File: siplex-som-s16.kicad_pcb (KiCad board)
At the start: 8 copper layers, 31.6 x 31.6 mm, 64 parts, among them J1 RFShield_OnePiece, J5 Conn_01x22, J7 Conn_01x22, J8 Conn_01x22, J9 Conn_01x22, U1 STM32H743IIKx, U2 IS42S16160J-6BLI, U3 W25Q32JVZP, U5 W25Q32JVZP, U7 TPS562200, Y1 25MHz, Y2 32.768KHz

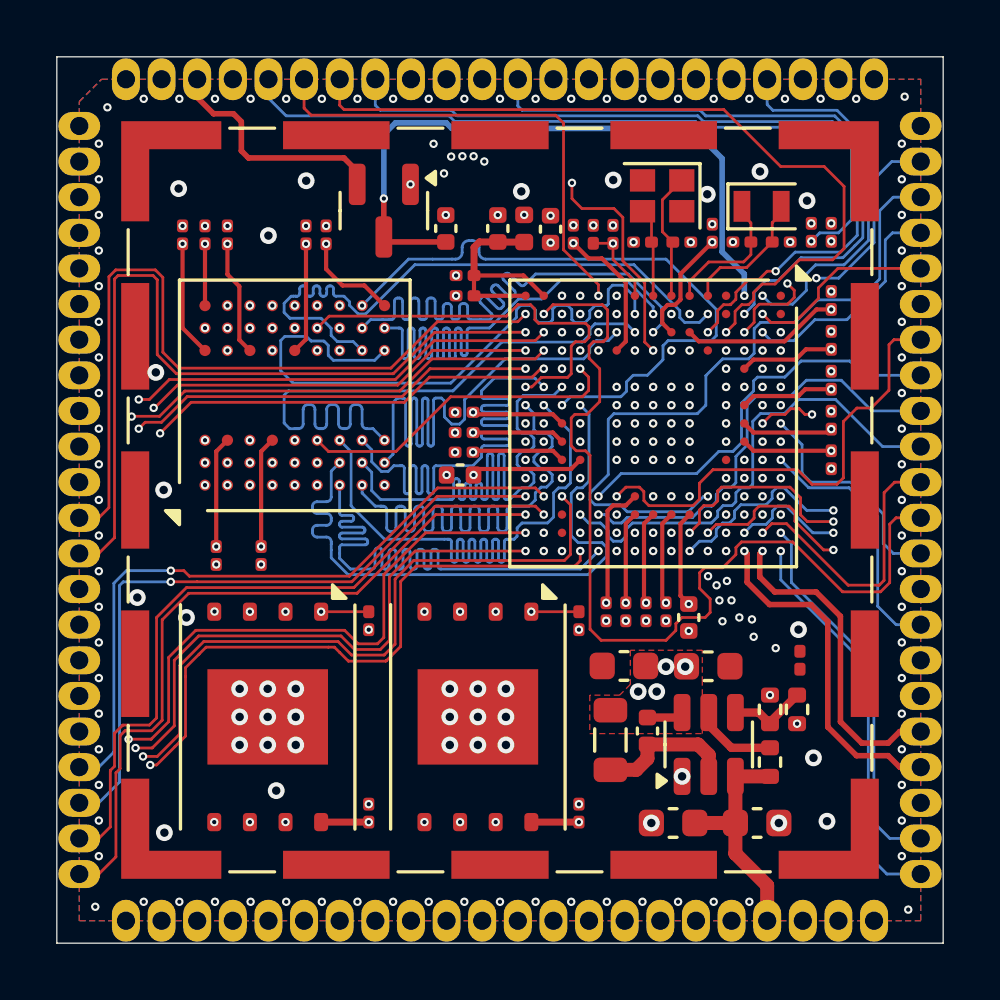
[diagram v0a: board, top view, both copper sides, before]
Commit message: Adding JLCPCB Part #
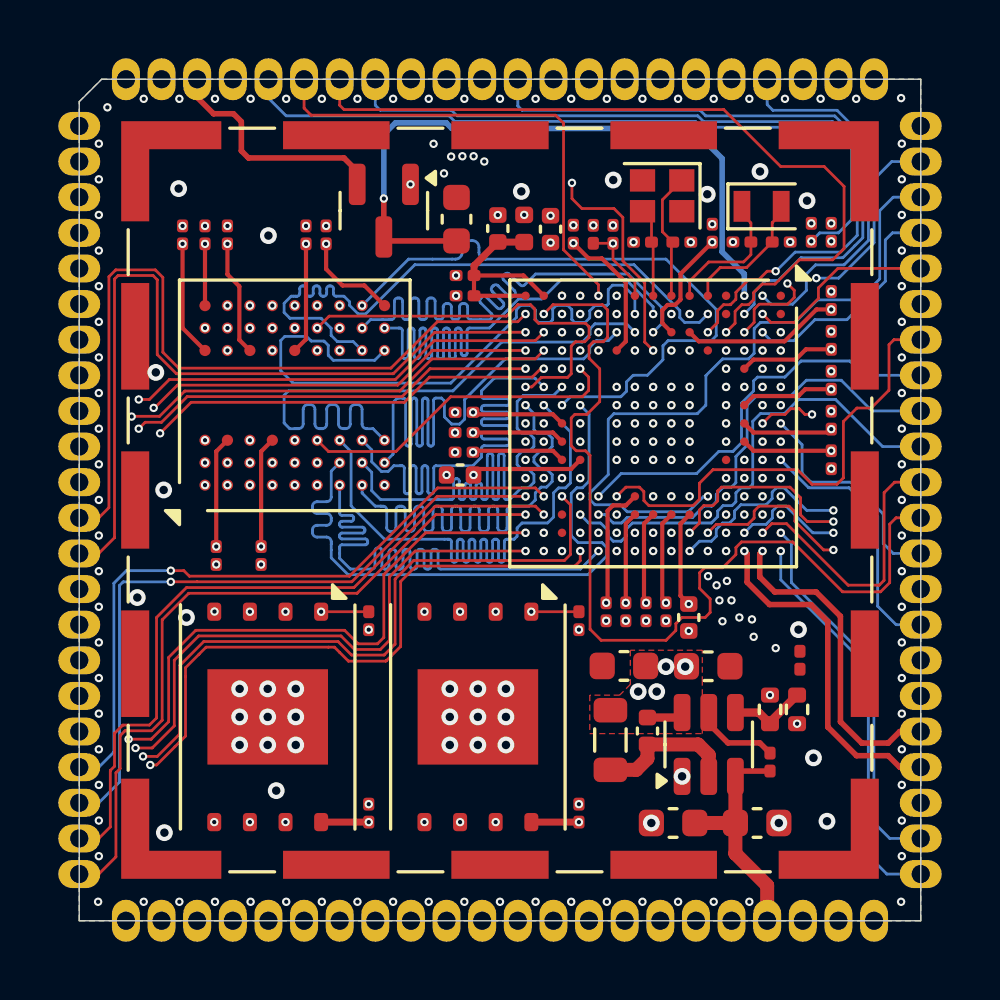
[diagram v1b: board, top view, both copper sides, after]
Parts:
- C10: footprint Capacitor_SMD:C_0402_1005Metric -> Capacitor_SMD:C_0603_1608Metric
- C43: value 100n -> 100n/0402
- L2: value 2u2 -> 2u2H
- R6: footprint Resistor_SMD:R_0402_1005Metric -> Resistor_SMD:R_0201_0603Metric
- moved C10 0.50 mm to (138.8, 88.1)
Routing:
- net GND: vias 208 -> 206
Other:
- board size 31.6 x 31.6 mm -> 30 x 30 mm

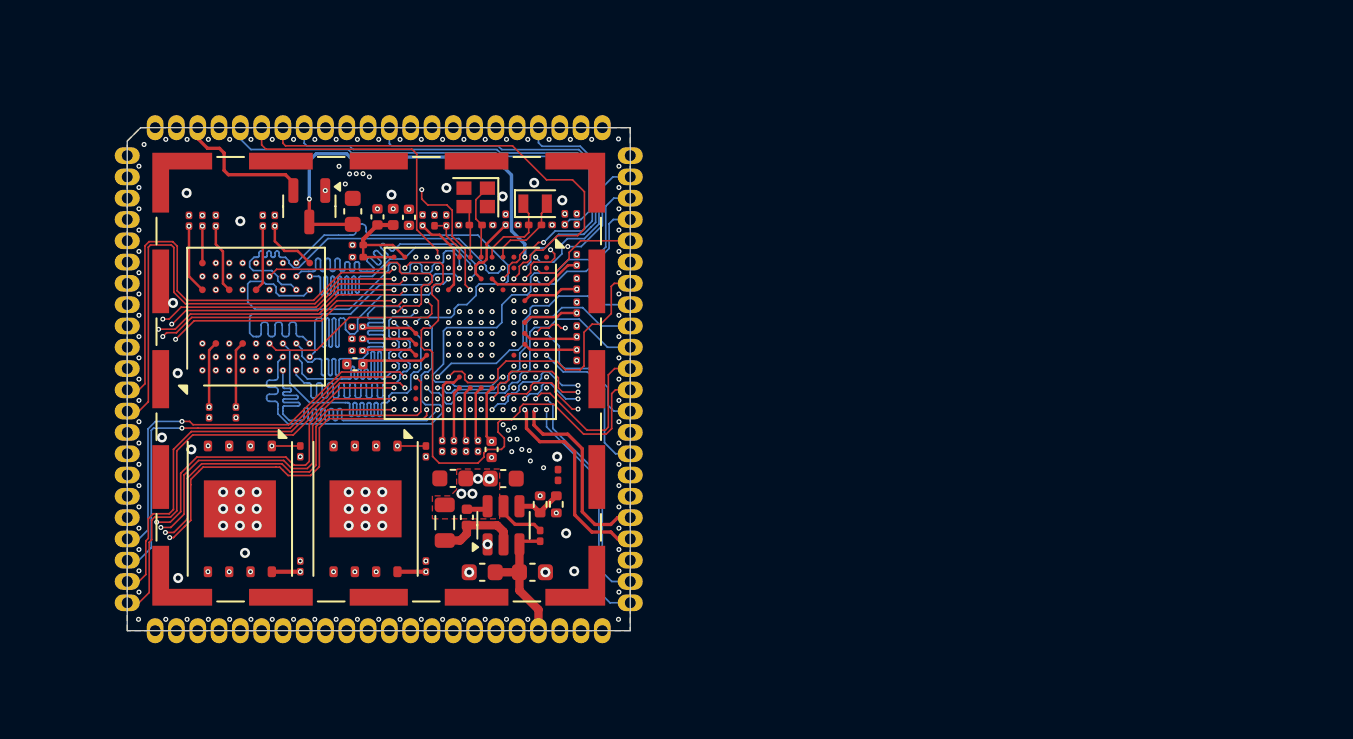
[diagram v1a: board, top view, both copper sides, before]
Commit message: Optimize layout with lowest impedance as possible
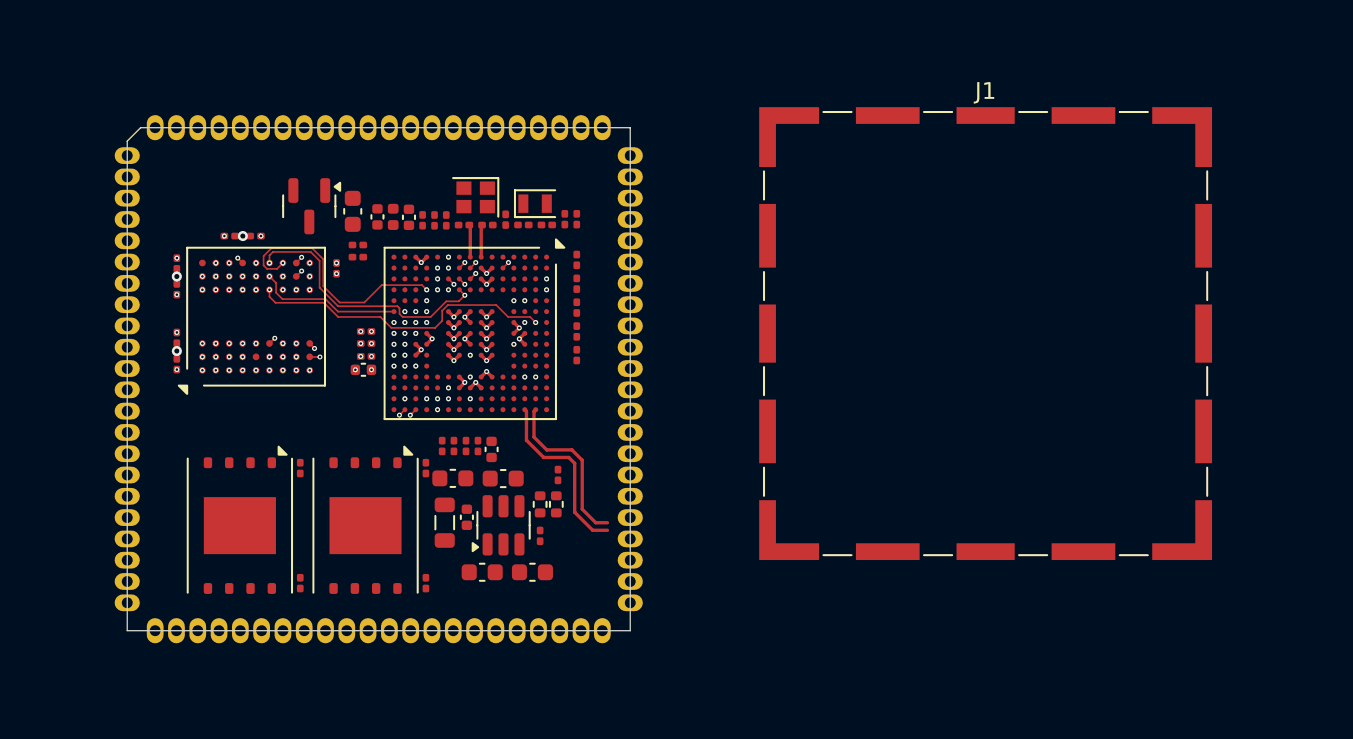
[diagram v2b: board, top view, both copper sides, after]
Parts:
- C4, C5: value 22p -> 12p
- C6, C7: value 22p -> 10p
- moved J1 36.3 mm to (176.5, 95.4), turned to 0 degrees
- moved C29 5.67 mm to (128.3, 95.6), turned to -90 degrees
- moved C28 4.65 mm to (137.8, 91.5), turned to 90 degrees
- moved C32 4.15 mm to (128.3, 92.7), turned to 90 degrees
- moved C26 3.46 mm to (128.3, 97.2)
- moved C33 2.97 mm to (128.3, 91.2)
- moved C27 1.24 mm to (131.4, 89.5), turned to 0 degrees
- moved C30 1.01 mm to (133.0, 89.5), turned to 180 degrees
- moved C31 1.00 mm to (135.6, 110.2)
- moved C38 1.00 mm to (143.1, 110.2)
- moved R4 1.00 mm to (135.6, 103.4)
- moved R5 1.00 mm to (143.1, 103.4)
- moved U3 1.00 mm to (132.0, 106.8)
- moved U5 1.00 mm to (139.5, 106.8)
- moved C11 0.63 mm to (139.6, 96.7)
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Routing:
- net +3V3: track 81.9 -> 7.36 mm, vias 35 -> 22
- net /Castellated_holes/LTDC_CLK: track 40.9 -> 0.00 mm, vias 1 -> 0
- net PB7: track 39.6 -> 0.00 mm, vias 1 -> 0
- net PB9: track 39.2 -> 0.00 mm, vias 1 -> 0
- net PB5: track 39.1 -> 0.00 mm, vias 1 -> 0
- net PB8: track 38.2 -> 0.00 mm, vias 1 -> 0
- net /MCU/~{FLASH_BK2_CS}: track 37.1 -> 0.00 mm, vias 2 -> 0
- net /MCU/BOOT0: track 34.0 -> 0.00 mm, vias 2 -> 0
- net /MCU/FLASH_BK2_IO0: track 33.8 -> 0.00 mm, vias 2 -> 0
- net /MCU/~{FLASH_BK1_CS}: track 33.8 -> 0.00 mm, vias 2 -> 0
- net /Castellated_holes/LTDC_R1: track 33.8 -> 0.00 mm, vias 1 -> 0
- net /MCU/FLASH_BK2_IO1: track 33.8 -> 0.00 mm, vias 2 -> 0
- net /MCU/FLASH_BK2_IO3: track 33.7 -> 0.00 mm, vias 2 -> 0
- net /MCU/FLASH_BK2_IO2: track 33.7 -> 0.00 mm, vias 2 -> 0
- net PD7: track 32.7 -> 0.00 mm, vias 2 -> 0
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- removed copper zone on F.Cu, net +3V3
- removed copper zone on B.Cu, net GND
- removed copper zone on F.Cu, net GND
- removed copper zone on In1.Cu, net GND
- removed copper zone on In3.Cu, net GND
- removed copper zone on In4.Cu, net GND
- removed copper zone on In6.Cu, net GND

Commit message: Finished LTDC tracks
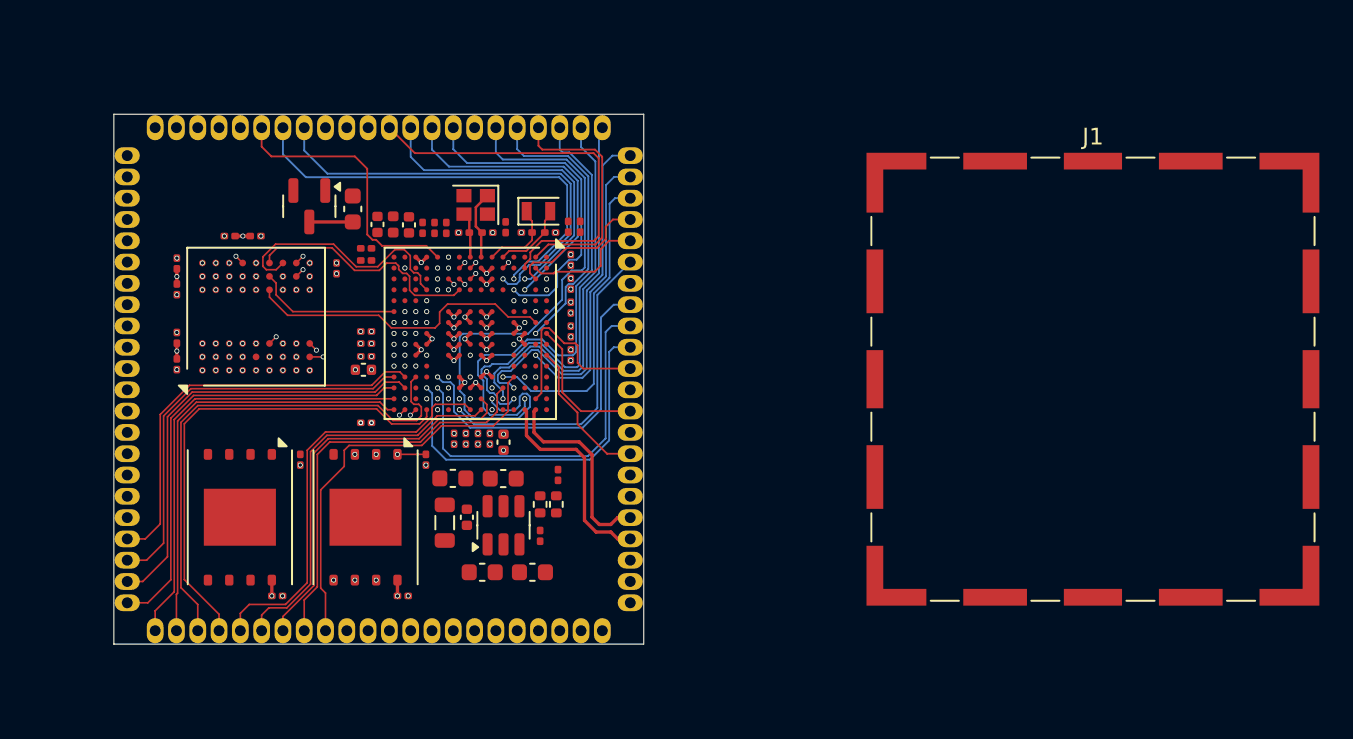
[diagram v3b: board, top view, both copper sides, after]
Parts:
- added R9: 22R, Resistor_SMD:R_0201_0603Metric, F.Cu at (139.6, 100.7)
- moved C38 8.90 mm to (134.3, 111.0), turned to 0 degrees
- moved R4 7.51 mm to (143.1, 102.9)
- moved R5 7.51 mm to (135.6, 102.9)
- moved U3 7.51 mm to (139.5, 106.3)
- moved U5 7.51 mm to (132.0, 106.3)
- moved J1 6.95 mm to (182.9, 98.1)
- moved C31 6.16 mm to (141.7, 111.0), turned to 0 degrees
- moved C2 0.83 mm to (147.8, 101.8)
- moved C17 0.83 mm to (144.8, 101.6)
- moved C18 0.83 mm to (145.5, 101.6)
- moved C22 0.83 mm to (146.2, 101.6)
- moved C23 0.83 mm to (146.9, 101.6)
- moved C39 0.53 mm to (139.6, 91.0)
- moved C9 0.53 mm to (139.6, 90.3)
- moved C6 0.49 mm to (150.5, 89.3)
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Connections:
- U3 pad 6: /MCU/FLASH_CLK -> Net-(U3-CLK)
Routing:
- net /Castellated_holes/LTDC_CLK: track 0.00 -> 37.5 mm, vias 0 -> 1
- net /Castellated_holes/LTDC_B2: track 0.00 -> 35.6 mm, vias 0 -> 1
- net PH7: track 0.00 -> 30.9 mm
- net PD13: track 0.00 -> 29.0 mm
- net /Castellated_holes/LTDC_G7: track 0.00 -> 27.9 mm, vias 0 -> 1
- net /Castellated_holes/LTDC_B3: track 0.00 -> 27.5 mm, vias 0 -> 1
- net PB11: track 0.00 -> 26.9 mm
- net /Castellated_holes/LTDC_HSYNC: track 0.00 -> 26.7 mm, vias 0 -> 1
- net PB14: track 0.00 -> 26.7 mm
- net /Castellated_holes/LTDC_VSYNC: track 0.00 -> 26.6 mm, vias 0 -> 1
- net PB13: track 0.00 -> 26.5 mm
- net PB15: track 0.00 -> 26.1 mm
- net /Castellated_holes/LTDC_G6: track 0.00 -> 25.6 mm, vias 0 -> 1
- net PC6: track 0.00 -> 25.0 mm
- net PB10: track 0.00 -> 24.9 mm
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- added copper zone on In1.Cu, net GND
- added copper zone on In4.Cu, net GND
- added copper zone on In6.Cu, net GND
- removed copper zone on In4.Cu, net +3V3
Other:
- board size 30 x 30 mm -> 31.6 x 31.6 mm

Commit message: SDRAM finished, changed castellated to 23pin each side, few pins unconnected
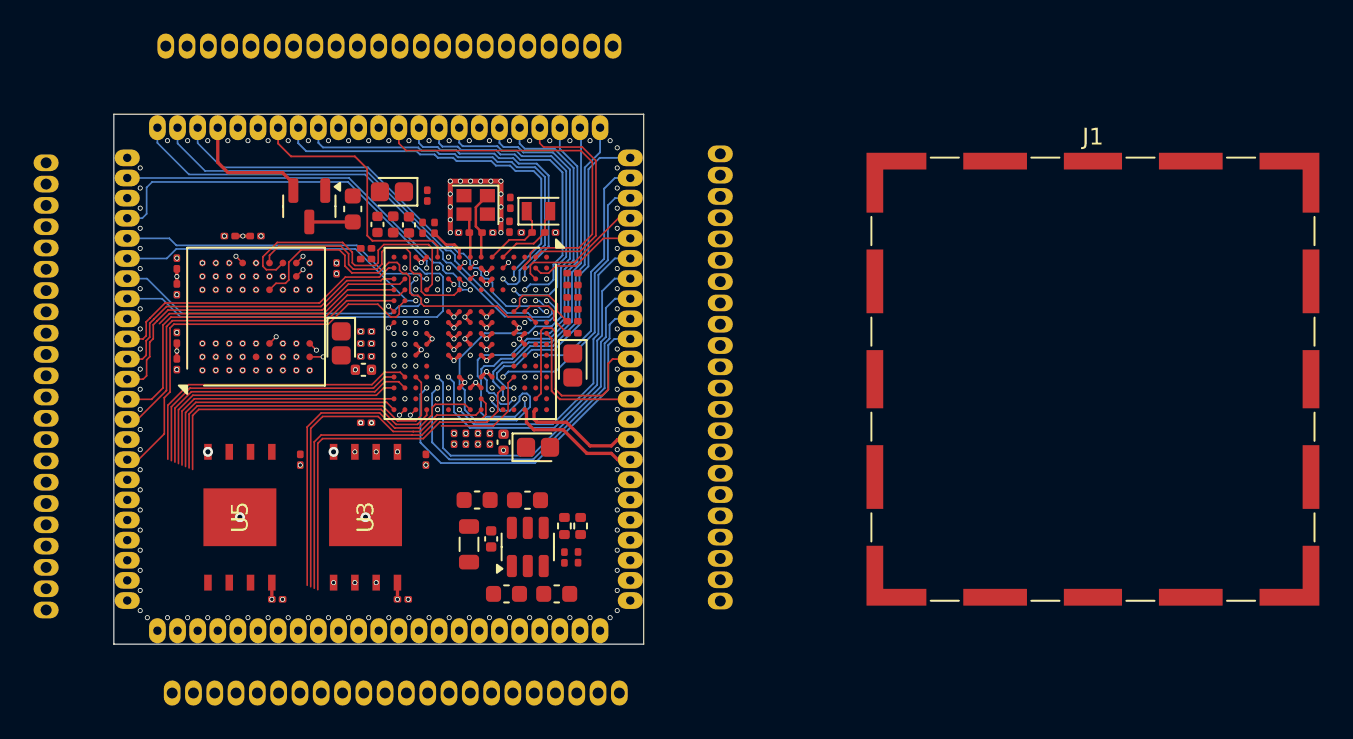
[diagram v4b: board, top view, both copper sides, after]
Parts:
- added C35: 1uF, Capacitor_Tantalum_SMD:CP_EIA-1608-08_AVX-J, F.Cu at (141.1, 86.9)
- added C37: 1uF, Capacitor_Tantalum_SMD:CP_EIA-1608-08_AVX-J, F.Cu at (149.8, 102.1)
- added C41: 1uF, Capacitor_Tantalum_SMD:CP_EIA-1608-08_AVX-J, F.Cu at (138.1, 95.9)
- added C45: 1uF, Capacitor_Tantalum_SMD:CP_EIA-1608-08_AVX-J, F.Cu at (151.9, 97.3)
- added J2: Conn_01x23, castellated_holes_header:castellated_01x23_P1.2mm, F.Cu at (155.3, 111.3)
- added J3: Conn_01x23, castellated_holes_header:castellated_01x23_P1.2mm, F.Cu at (127.1, 83.1)
- added J4: Conn_01x23, castellated_holes_header:castellated_01x23_P1.2mm, F.Cu at (125.3, 84.9)
- added J6: Conn_01x23, castellated_holes_header:castellated_01x23_P1.2mm, F.Cu at (127.1, 113.1)
- U3, U5: footprint Package_SON:WSON-8-1EP_8x6mm_P1.27mm_EP3.4x4.3mm -> W25Q256JVEIQ:SON127P800X600X80-9N
- moved R1 6.36 mm to (151.9, 95.3), turned to 180 degrees
- moved R3 5.64 mm to (151.9, 94.6), turned to 180 degrees
- moved J5 5.37 mm to (160.7, 111.3)
- moved C15 5.05 mm to (152.2, 108.7)
- moved C16 4.96 mm to (148.2, 87.6)
- moved J7 4.91 mm to (127.6, 78.2)
- moved J8 4.86 mm to (120.5, 85.2)
- moved J9 3.85 mm to (128.0, 116.8)
- moved C24 2.73 mm to (151.9, 93.9), turned to 180 degrees
- moved C25 2.03 mm to (151.9, 93.2), turned to 180 degrees
- moved R2 1.98 mm to (143.2, 87.1)
- moved C34 1.94 mm to (150.9, 110.9)
- moved C36 1.94 mm to (146.2, 105.3)
- moved C42 1.94 mm to (147.9, 110.9)
- moved C44 1.94 mm to (149.2, 105.3)
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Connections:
- J5 pad 1: /Castellated_holes/SWDIO -> unconnected-(J5-Pin_1-Pad1)
- J5 pad 10: /Castellated_holes/LTDC_R0 -> unconnected-(J5-Pin_10-Pad10)
- J5 pad 11: /Castellated_holes/LTDC_R1 -> unconnected-(J5-Pin_11-Pad11)
- J5 pad 12: /Castellated_holes/LTDC_R2 -> unconnected-(J5-Pin_12-Pad12)
- J5 pad 13: /Castellated_holes/LTDC_R3 -> unconnected-(J5-Pin_13-Pad13)
- J5 pad 14: /Castellated_holes/LTDC_R4 -> unconnected-(J5-Pin_14-Pad14)
- J5 pad 15: /Castellated_holes/LTDC_R5 -> unconnected-(J5-Pin_15-Pad15)
- J5 pad 16: /Castellated_holes/LTDC_R6 -> unconnected-(J5-Pin_16-Pad16)
- J5 pad 17: /Castellated_holes/LTDC_R7 -> unconnected-(J5-Pin_17-Pad17)
- J5 pad 18: /Castellated_holes/LTDC_G0 -> unconnected-(J5-Pin_18-Pad18)
- J5 pad 19: /Castellated_holes/LTDC_G1 -> unconnected-(J5-Pin_19-Pad19)
- J5 pad 2: /Castellated_holes/SWCLK -> unconnected-(J5-Pin_2-Pad2)
- J5 pad 20: /Castellated_holes/LTDC_G2 -> unconnected-(J5-Pin_20-Pad20)
- J5 pad 21: /Castellated_holes/LTDC_G3 -> unconnected-(J5-Pin_21-Pad21)
- J5 pad 22: /Castellated_holes/LTDC_G4 -> unconnected-(J5-Pin_22-Pad22)
- J5 pad 3: GND -> unconnected-(J5-Pin_3-Pad3)
- J5 pad 4: /Castellated_holes/USB_DN -> unconnected-(J5-Pin_4-Pad4)
- J5 pad 5: /Castellated_holes/USB_DP -> unconnected-(J5-Pin_5-Pad5)
- J5 pad 6: GND -> unconnected-(J5-Pin_6-Pad6)
- J5 pad 7: /Castellated_holes/USB_VBUS_DET -> unconnected-(J5-Pin_7-Pad7)
- J5 pad 8: /Castellated_holes/SWO -> unconnected-(J5-Pin_8-Pad8)
- J5 pad 9: GND -> unconnected-(J5-Pin_9-Pad9)
- J7 pad 1: PB5 -> unconnected-(J7-Pin_1-Pad1)
- J7 pad 10: /Castellated_holes/LTDC_CLK -> unconnected-(J7-Pin_10-Pad10)
- J7 pad 11: GND -> unconnected-(J7-Pin_11-Pad11)
- J7 pad 12: /Castellated_holes/LTDC_B7 -> unconnected-(J7-Pin_12-Pad12)
- J7 pad 13: /Castellated_holes/LTDC_B6 -> unconnected-(J7-Pin_13-Pad13)
- J7 pad 14: /Castellated_holes/LTDC_B5 -> unconnected-(J7-Pin_14-Pad14)
- J7 pad 15: /Castellated_holes/LTDC_B4 -> unconnected-(J7-Pin_15-Pad15)
- J7 pad 16: /Castellated_holes/LTDC_B3 -> unconnected-(J7-Pin_16-Pad16)
- J7 pad 17: /Castellated_holes/LTDC_B2 -> unconnected-(J7-Pin_17-Pad17)
- J7 pad 18: /Castellated_holes/LTDC_B1 -> unconnected-(J7-Pin_18-Pad18)
- J7 pad 19: /Castellated_holes/LTDC_B0 -> unconnected-(J7-Pin_19-Pad19)
- J7 pad 2: GND -> unconnected-(J7-Pin_2-Pad2)
- J7 pad 20: /Castellated_holes/LTDC_G7 -> unconnected-(J7-Pin_20-Pad20)
- J7 pad 21: /Castellated_holes/LTDC_G6 -> unconnected-(J7-Pin_21-Pad21)
- J7 pad 22: /Castellated_holes/LTDC_G5 -> unconnected-(J7-Pin_22-Pad22)
- J7 pad 3: VRTC -> unconnected-(J7-Pin_3-Pad3)
- J7 pad 4: /Castellated_holes/NRST -> unconnected-(J7-Pin_4-Pad4)
- J7 pad 5: /MCU/BOOT0 -> unconnected-(J7-Pin_5-Pad5)
- J7 pad 6: /Castellated_holes/LTDC_DE -> unconnected-(J7-Pin_6-Pad6)
- J7 pad 7: /Castellated_holes/LTDC_VSYNC -> unconnected-(J7-Pin_7-Pad7)
- J7 pad 8: /Castellated_holes/LTDC_HSYNC -> unconnected-(J7-Pin_8-Pad8)
- J7 pad 9: GND -> unconnected-(J7-Pin_9-Pad9)
- J8 pad 1: PB7 -> unconnected-(J8-Pin_1-Pad1)
- J8 pad 10: PA1 -> unconnected-(J8-Pin_10-Pad10)
- J8 pad 11: PA4 -> unconnected-(J8-Pin_11-Pad11)
- J8 pad 12: PA3 -> unconnected-(J8-Pin_12-Pad12)
- J8 pad 13: PA7 -> unconnected-(J8-Pin_13-Pad13)
- J8 pad 14: PA6 -> unconnected-(J8-Pin_14-Pad14)
- J8 pad 15: PA5 -> unconnected-(J8-Pin_15-Pad15)
- J8 pad 16: PB0 -> unconnected-(J8-Pin_16-Pad16)
- J8 pad 17: PB1 -> unconnected-(J8-Pin_17-Pad17)
- J8 pad 18: PC5 -> unconnected-(J8-Pin_18-Pad18)
- J8 pad 19: PB12 -> unconnected-(J8-Pin_19-Pad19)
- J8 pad 2: PB8 -> unconnected-(J8-Pin_2-Pad2)
- J8 pad 20: PB10 -> unconnected-(J8-Pin_20-Pad20)
- J8 pad 21: PB13 -> unconnected-(J8-Pin_21-Pad21)
- J8 pad 22: PB11 -> unconnected-(J8-Pin_22-Pad22)
- J8 pad 3: PB9 -> unconnected-(J8-Pin_3-Pad3)
- J8 pad 4: PH4 -> unconnected-(J8-Pin_4-Pad4)
- J8 pad 5: GND -> unconnected-(J8-Pin_5-Pad5)
- J8 pad 6: PC0 -> unconnected-(J8-Pin_6-Pad6)
- J8 pad 7: PC1 -> unconnected-(J8-Pin_7-Pad7)
- J8 pad 8: PC4 -> unconnected-(J8-Pin_8-Pad8)
- J8 pad 9: PA0 -> unconnected-(J8-Pin_9-Pad9)
- J9 pad 1: PB14 -> unconnected-(J9-Pin_1-Pad1)
- J9 pad 10: PD3 -> unconnected-(J9-Pin_10-Pad10)
- J9 pad 11: PD5 -> unconnected-(J9-Pin_11-Pad11)
- J9 pad 12: PD6 -> unconnected-(J9-Pin_12-Pad12)
- J9 pad 13: PD7 -> unconnected-(J9-Pin_13-Pad13)
- J9 pad 14: PI3 -> unconnected-(J9-Pin_14-Pad14)
- J9 pad 15: PA15 -> unconnected-(J9-Pin_15-Pad15)
- J9 pad 16: PC12 -> unconnected-(J9-Pin_16-Pad16)
- J9 pad 17: PG11 -> unconnected-(J9-Pin_17-Pad17)
- J9 pad 18: PB4 -> unconnected-(J9-Pin_18-Pad18)
- J9 pad 19: VIN -> unconnected-(J9-Pin_19-Pad19)
- J9 pad 2: PB15 -> unconnected-(J9-Pin_2-Pad2)
- J9 pad 20: +3V3 -> unconnected-(J9-Pin_20-Pad20)
- J9 pad 21: GND -> unconnected-(J9-Pin_21-Pad21)
- J9 pad 22: GND -> unconnected-(J9-Pin_22-Pad22)
- J9 pad 3: PH7 -> unconnected-(J9-Pin_3-Pad3)
- J9 pad 4: PD13 -> unconnected-(J9-Pin_4-Pad4)
- J9 pad 5: PC6 -> unconnected-(J9-Pin_5-Pad5)
- J9 pad 6: PC7 -> unconnected-(J9-Pin_6-Pad6)
- J9 pad 7: PC8 -> unconnected-(J9-Pin_7-Pad7)
- J9 pad 8: PH14 -> unconnected-(J9-Pin_8-Pad8)
- J9 pad 9: PD2 -> unconnected-(J9-Pin_9-Pad9)
- U1 pad N13: unconnected-(U1-PD12-PadN13) -> PD12
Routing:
- net (no net): track 0.00 -> 122.0 mm
- net PB9: track 0.00 -> 33.8 mm, vias 0 -> 1
- net PB8: track 0.00 -> 30.5 mm, vias 0 -> 1
- net PB7: track 0.00 -> 29.3 mm, vias 0 -> 1
- net PB5: track 0.00 -> 26.5 mm, vias 0 -> 1
- net PC5: track 0.00 -> 24.9 mm
- net PA4: track 0.00 -> 24.0 mm, vias 0 -> 1
- net PH4: track 0.00 -> 23.6 mm, vias 0 -> 1
- net PA1: track 0.00 -> 23.3 mm, vias 0 -> 1
- net PC0: track 0.00 -> 22.1 mm, vias 0 -> 1
- net PA5: track 0.00 -> 21.5 mm
- net PB0: track 0.00 -> 21.1 mm
- net PA0: track 0.00 -> 20.6 mm, vias 0 -> 1
- net PA6: track 0.00 -> 20.6 mm
- net PA7: track 0.00 -> 18.9 mm
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- added copper zone on In3.Cu, net +3V3
